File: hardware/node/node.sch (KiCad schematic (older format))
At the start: 65 parts, among them J1 BOOT0_Jumper, J2 FTDI, J3 SMA Female, J4 2 x AA, J5 SWD, Q1 Si2323DDS, SW1 DTSM-65R-V-B, SW2 DTSM-65R-V-B, U1 RFM69HW, U2 SHTC3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

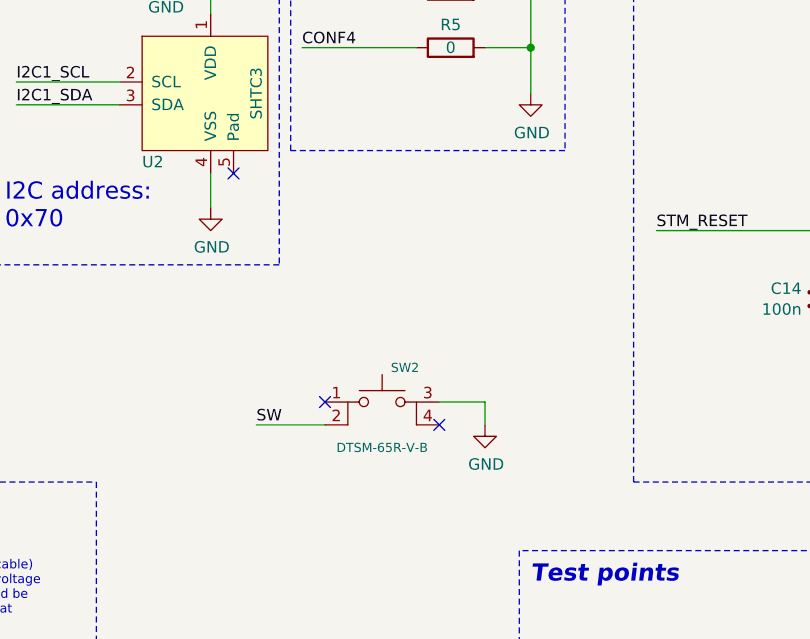
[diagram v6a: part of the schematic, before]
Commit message: Cleaned up schematic
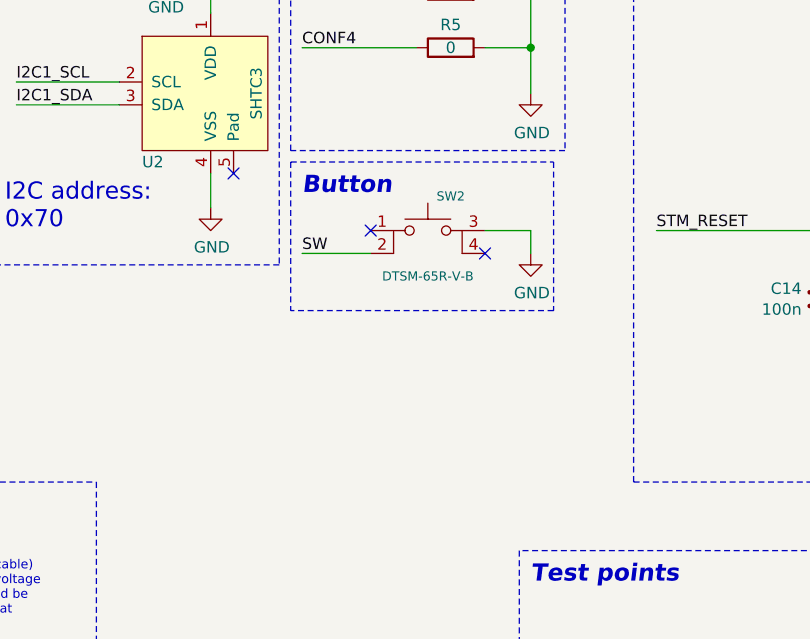
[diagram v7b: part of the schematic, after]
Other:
- note added: "Button"
- moved on the sheet: SW2
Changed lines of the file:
@@
 L humidity:SW_Push_4pin SW2
 U 1 1 5D4CC3C1
-P 8350 3400
-F 0 "SW2" H 8450 3550 40  0000 C CNN
-F 1 "DTSM-65R-V-B" H 8350 3200 40  0000 C CNN
-F 2 "humidity:SW_SPST_DTSM-6" H 8350 3400 40  0001 C CNN
-F 3 "https://www.tme.eu/se/en/details/dtsm-65r-v-b/microswitches-tact/diptronics/" H 8350 3400 40  0001 C CNN
-F 4 "https://www.tme.eu/se/en/details/dtsm-65r-v-b/microswitches-tact/diptronics/" H -2300 850 50  0001 C CNN "TME Link"
-F 5 "1.8894" H -2300 850 50  0001 C CNN "TME Price"
-	1    8350 3400
+P 8550 2650
+F 0 "SW2" H 8650 2800 40  0000 C CNN
+F 1 "DTSM-65R-V-B" H 8550 2450 40  0000 C CNN
+F 2 "humidity:SW_SPST_DTSM-6" H 8550 2650 40  0001 C CNN
+F 3 "https://www.tme.eu/se/en/details/dtsm-65r-v-b/microswitches-tact/diptronics/" H 8550 2650 40  0001 C CNN
+F 4 "https://www.tme.eu/se/en/details/dtsm-65r-v-b/microswitches-tact/diptronics/" H -2100 100 50  0001 C CNN "TME Link"
+F 5 "1.8894" H -2100 100 50  0001 C CNN "TME Price"
+	1    8550 2650
 	1    0    0    -1
 $EndComp
@@
 L power:GND #PWR0103
 U 1 1 5D4DD0C9
-P 8800 3500
-F 0 "#PWR0103" H 8800 3250 50  0001 C CNN
-F 1 "GND" H 8805 3327 50  0000 C CNN
-F 2 "" H 8800 3500 50  0001 C CNN
-F 3 "" H 8800 3500 50  0001 C CNN
-	1    8800 3500
+P 9000 2750
+F 0 "#PWR0103" H 9000 2500 50  0001 C CNN
+F 1 "GND" H 9005 2577 50  0000 C CNN
+F 2 "" H 9000 2750 50  0001 C CNN
+F 3 "" H 9000 2750 50  0001 C CNN
+	1    9000 2750
 	1    0    0    -1
 $EndComp
 Wire Wire Line
-	8800 3500 8800 3400
+	9000 2750 9000 2650
 Wire Wire Line
-	8800 3400 8600 3400
+	9000 2650 8800 2650
 Wire Wire Line
-	8100 3500 7800 3500
-NoConn ~ 8600 3500
-NoConn ~ 8100 3400
-Text Label 7800 3500 0    50   ~ 0
+	8300 2750 8000 2750
+NoConn ~ 8800 2750
+NoConn ~ 8300 2650
+Text Label 8000 2750 0    50   ~ 0
 SW
 Wire Wire Line
 	11000 2750 10900 2750
+Text Notes 8000 2500 0    75   Italic 15
+Button
+Wire Notes Line
+	7950 2350 9100 2350
+Wire Notes Line
+	9100 2350 9100 3000
+Wire Notes Line
+	9100 3000 7950 3000
+Wire Notes Line
+	7950 2350 7950 3000
 $EndSCHEMATC

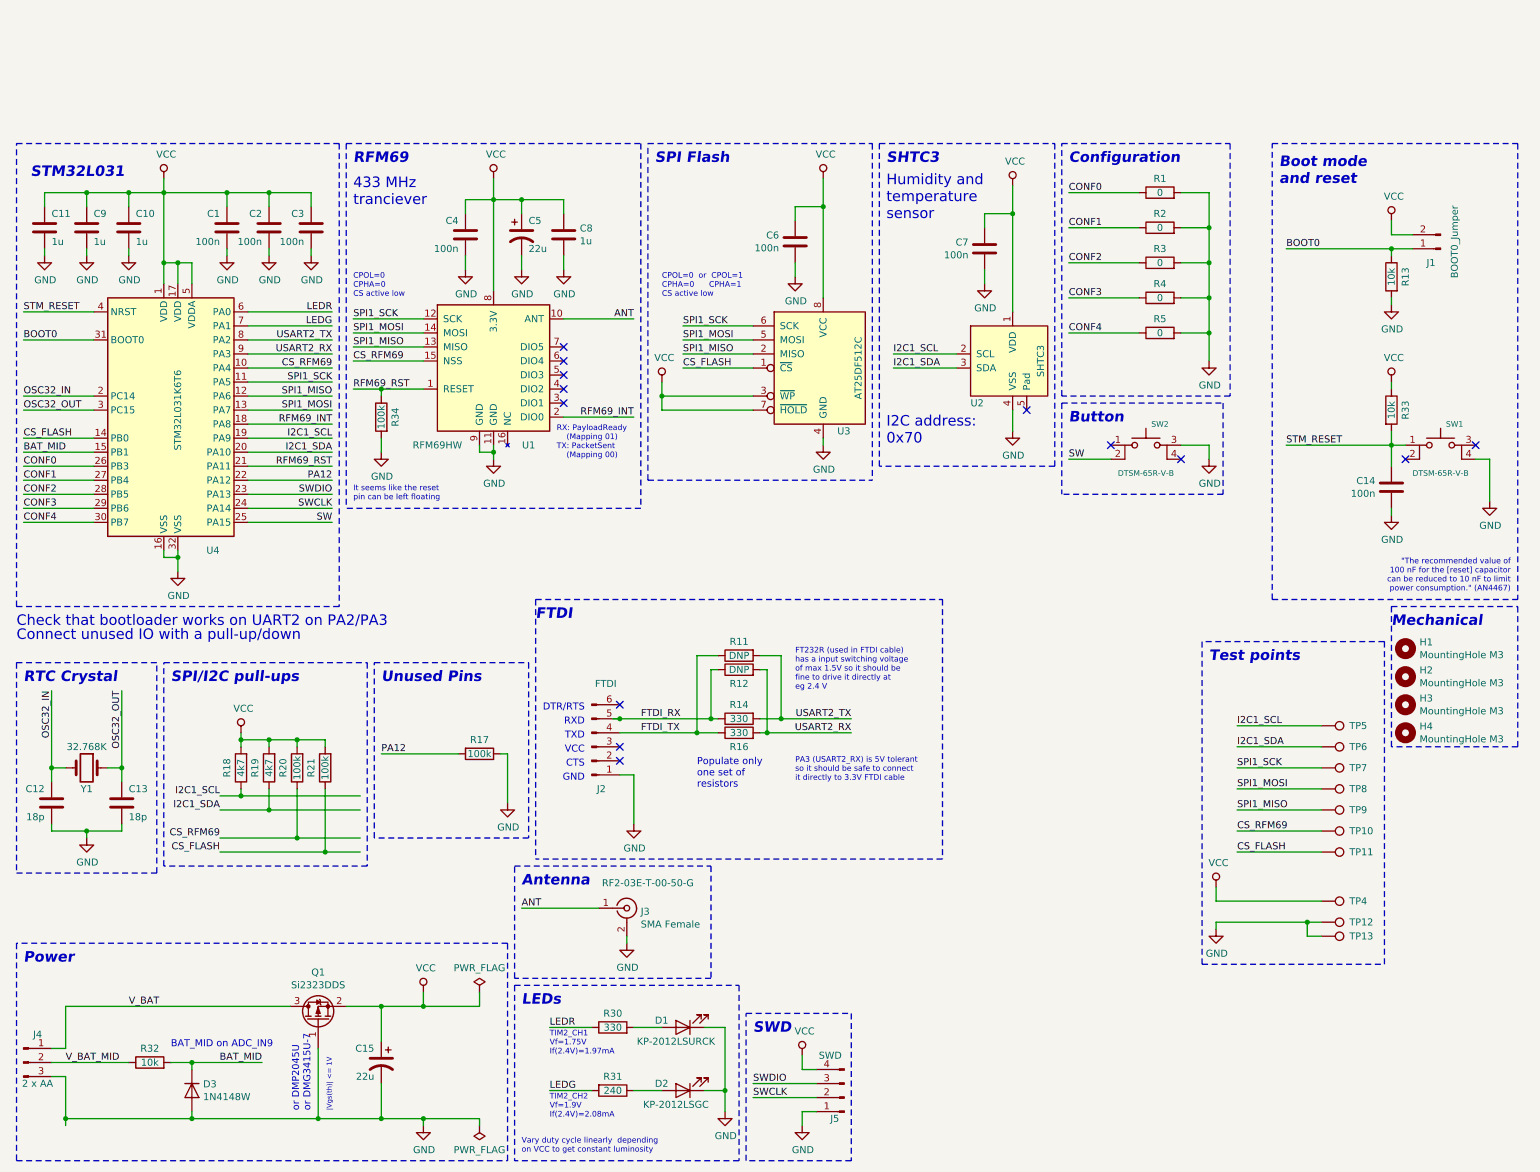
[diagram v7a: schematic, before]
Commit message: Exchanged pins LEDR (PA0) <-> SW (PA15)
LEDR is still on TIM2_CH1
SW is now on WKUP1 and can hence be used to exit the mcu from standby
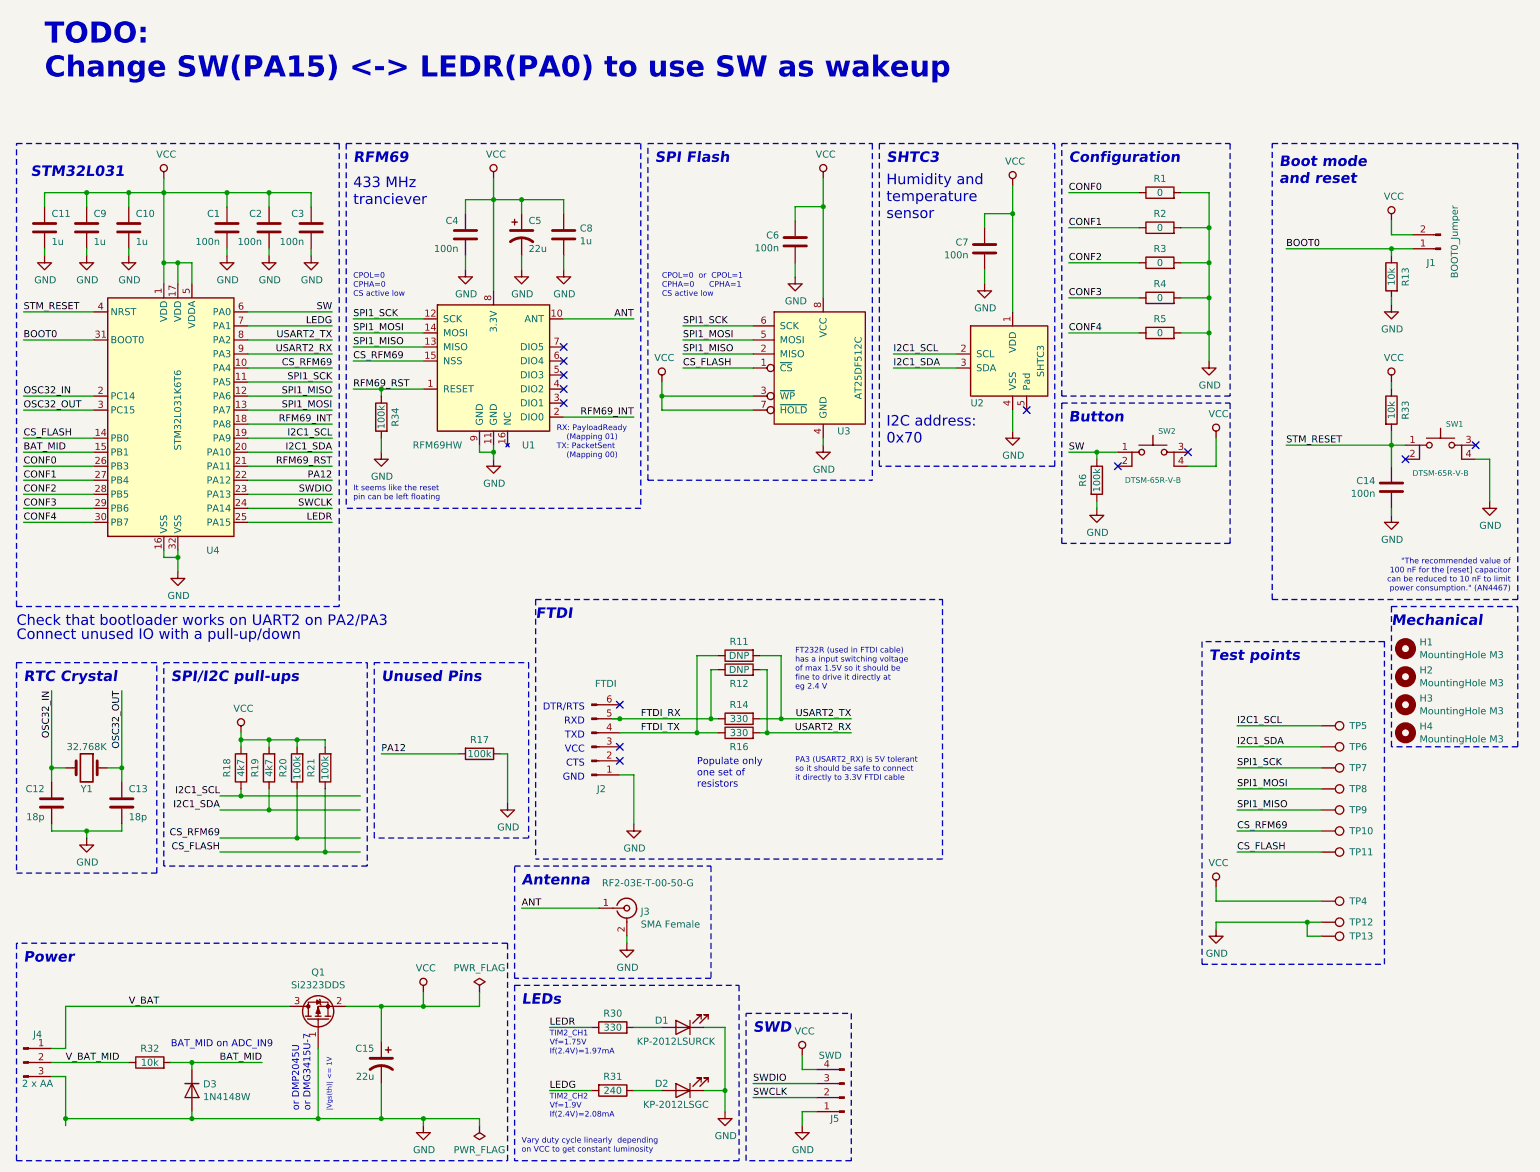
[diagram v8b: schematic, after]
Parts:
- added R6: 100k, Resistor_SMD:R_0603_1608Metric_Pad1.05x0.95mm_HandSolder, symbol Device:R
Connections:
- net GND: now also R6.2; no longer SW2.3
- net LEDR: now also U4.25 (PA15); no longer U4.6 (PA0)
- net SW: now also SW2.1, U4.6 (PA0), R6.1; no longer SW2.2, U4.25 (PA15)
- net VCC: now also SW2.4
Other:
- note added: "TODO:\nChange SW(PA15) <-> LEDR(PA0) to use SW as wakeup"
- moved on the sheet: SW2
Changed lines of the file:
@@
 Wire Wire Line
 	2150 1800 2750 1800
-Text Label 2750 1700 2    50   ~ 0
+Text Label 2750 3200 2    50   ~ 0
 LEDR
 Wire Wire Line
@@
 Wire Wire Line
 	2150 3200 2750 3200
-Text Label 2750 3200 2    50   ~ 0
+Text Label 2750 1700 2    50   ~ 0
 SW
 $Comp
@@
 L humidity:SW_Push_4pin SW2
 U 1 1 5D4CC3C1
-P 8550 2650
-F 0 "SW2" H 8650 2800 40  0000 C CNN
-F 1 "DTSM-65R-V-B" H 8550 2450 40  0000 C CNN
-F 2 "humidity:SW_SPST_DTSM-6" H 8550 2650 40  0001 C CNN
-F 3 "https://www.tme.eu/se/en/details/dtsm-65r-v-b/microswitches-tact/diptronics/" H 8550 2650 40  0001 C CNN
-F 4 "https://www.tme.eu/se/en/details/dtsm-65r-v-b/microswitches-tact/diptronics/" H -2100 100 50  0001 C CNN "TME Link"
-F 5 "1.8894" H -2100 100 50  0001 C CNN "TME Price"
-	1    8550 2650
+P 8600 2700
+F 0 "SW2" H 8700 2850 40  0000 C CNN
+F 1 "DTSM-65R-V-B" H 8600 2500 40  0000 C CNN
+F 2 "humidity:SW_SPST_DTSM-6" H 8600 2700 40  0001 C CNN
+F 3 "https://www.tme.eu/se/en/details/dtsm-65r-v-b/microswitches-tact/diptronics/" H 8600 2700 40  0001 C CNN
+F 4 "https://www.tme.eu/se/en/details/dtsm-65r-v-b/microswitches-tact/diptronics/" H -2050 150 50  0001 C CNN "TME Link"
+F 5 "1.8894" H -2050 150 50  0001 C CNN "TME Price"
+	1    8600 2700
 	1    0    0    -1
 $EndComp
@@
 L power:GND #PWR0103
 U 1 1 5D4DD0C9
-P 9000 2750
-F 0 "#PWR0103" H 9000 2500 50  0001 C CNN
-F 1 "GND" H 9005 2577 50  0000 C CNN
-F 2 "" H 9000 2750 50  0001 C CNN
-F 3 "" H 9000 2750 50  0001 C CNN
-	1    9000 2750
-	1    0    0    -1
-$EndComp
-Wire Wire Line
-	9000 2750 9000 2650
-Wire Wire Line
-	9000 2650 8800 2650
-Wire Wire Line
-	8300 2750 8000 2750
-NoConn ~ 8800 2750
-NoConn ~ 8300 2650
-Text Label 8000 2750 0    50   ~ 0
+P 8200 3100
+F 0 "#PWR0103" H 8200 2850 50  0001 C CNN
+F 1 "GND" H 8205 2927 50  0000 C CNN
+F 2 "" H 8200 3100 50  0001 C CNN
+F 3 "" H 8200 3100 50  0001 C CNN
+	1    8200 3100
+	1    0    0    -1
+$EndComp
+NoConn ~ 8850 2700
+NoConn ~ 8350 2800
+Text Label 8000 2700 0    50   ~ 0
 SW
 Wire Wire Line
@@
 Button
 Wire Notes Line
-	7950 2350 9100 2350
-Wire Notes Line
-	9100 2350 9100 3000
-Wire Notes Line
-	9100 3000 7950 3000
-Wire Notes Line
-	7950 2350 7950 3000
+	7950 2350 9150 2350
+Wire Notes Line
+	9150 2350 9150 3350
+Wire Notes Line
+	9150 3350 7950 3350
+Wire Notes Line
+	7950 2350 7950 3350
+Text Notes 700  50   0    150  ~ 30
+TODO:\nChange SW(PA15) <-> LEDR(PA0) to use SW as wakeup
+Wire Wire Line
+	8350 2700 8200 2700
+Wire Wire Line
+	9050 2800 8850 2800
+$Comp
+L power:VCC #PWR0104
+U 1 1 5D5C76F0
+P 9050 2600
+F 0 "#PWR0104" H 9050 2450 50  0001 C CNN
+F 1 "VCC" H 9067 2773 50  0000 C CNN
+F 2 "" H 9050 2600 50  0001 C CNN
+F 3 "" H 9050 2600 50  0001 C CNN
+	1    9050 2600
+	1    0    0    -1
+$EndComp
+Wire Wire Line
+	9050 2600 9050 2800
+Wire Wire Line
+	8200 2750 8200 2700
+Connection ~ 8200 2700
+Wire Wire Line
+	8200 2700 8000 2700
+Wire Wire Line
+	8200 3100 8200 3050
+$Comp
+L Device:R R6
+U 1 1 5D6B13F6
+P 8200 2900
+F 0 "R6" V 8100 2900 50  0000 C CNN
+F 1 "100k" V 8200 2900 50  0000 C CNN
+F 2 "Resistor_SMD:R_0603_1608Metric_Pad1.05x0.95mm_HandSolder" V 8130 2900 50  0001 C CNN
+F 3 "~" H 8200 2900 50  0001 C CNN
+F 4 "https://www.tme.eu/se/en/details/cq0603-100k-1%25/0603-smd-resistors/royal-ohm/cq03saf1003t5e/" H 4400 -1950 50  0001 C CNN "TME Link"
+F 5 "0.18525" H 4400 -1950 50  0001 C CNN "TME Price"
+	1    8200 2900
+	1    0    0    -1
+$EndComp
 $EndSCHEMATC
